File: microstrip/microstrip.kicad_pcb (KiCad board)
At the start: 2 copper layers, 50 x 50 mm, 2 parts

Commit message: Adding some changes to the design, modeling and simulation config files.
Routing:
- removed copper zone on F.Cu, net GND
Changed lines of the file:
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@@
 		(pad "" smd rect
 			(at 0 0)
-			(size 1.5 1.5)
+			(size 2.85 2.85)
 			(layers "F.Cu" "F.Mask")
 			(net 2 "50R")
@@
 		(pad "" smd rect
 			(at 0 0)
-			(size 1.5 1.5)
+			(size 2.85 2.85)
 			(layers "F.Cu" "F.Mask")
 			(net 2 "50R")
@@
 		(end 89.445 75)
 		(stroke
-			(width 1.275)
+			(width 2.85)
 			(type solid)
 		)
@@
 		(layer "Dwgs.User")
 		(pts
-			(xy 83.78 75.64) (xy 83.78 75.89)
-		)
-		(height 19.63)
-		(orientation 1)
-		(format
-			(prefix "")
-			(suffix "mm")
-			(units 3)
-			(units_format 0)
-			(precision 4)
-			(suppress_zeroes yes)
-		)
-		(style
-			(thickness 0.2)
-			(arrow_length 1.27)
-			(text_position_mode 2)
-			(arrow_direction outward)
-			(extension_height 0.58642)
-			(extension_offset 0.5)
-			(keep_text_aligned yes)
-		)
-		(gr_text "0.25mm"
-			(at 105.46 75.74 90)
-			(layer "Dwgs.User")
-			(effects
-				(font
-					(size 1.5 1.5)
-					(thickness 0.3)
-				)
-			)
-		)
-	)
-	(dimension
-		(type orthogonal)
-		(layer "Dwgs.User")
-		(pts
-			(xy 62.54 74.36) (xy 62.54 75.64)
+			(xy 58.430002 73.574998) (xy 58.429968 76.425074)
 		)
 		(height -17.54)
@@
 			(units 3)
 			(units_format 0)
-			(precision 5)
-			(override_value "1.275")
+			(precision 2)
+			(suppress_zeroes yes)
 		)
 		(style
@@
 			(keep_text_aligned yes)
 		)
-		(gr_text "1.275mm"
-			(at 43.2 75 90)
+		(gr_text "2.85mm"
+			(at 39.090002 75.000036 90)
 			(layer "Dwgs.User")
 			(effects
@@
 		(net_name "GND")
 		(locked yes)
-		(layers "F.Cu" "B.Cu")
+		(layer "B.Cu")
 		(name "gnd_plane")
 		(hatch edge 0.5)

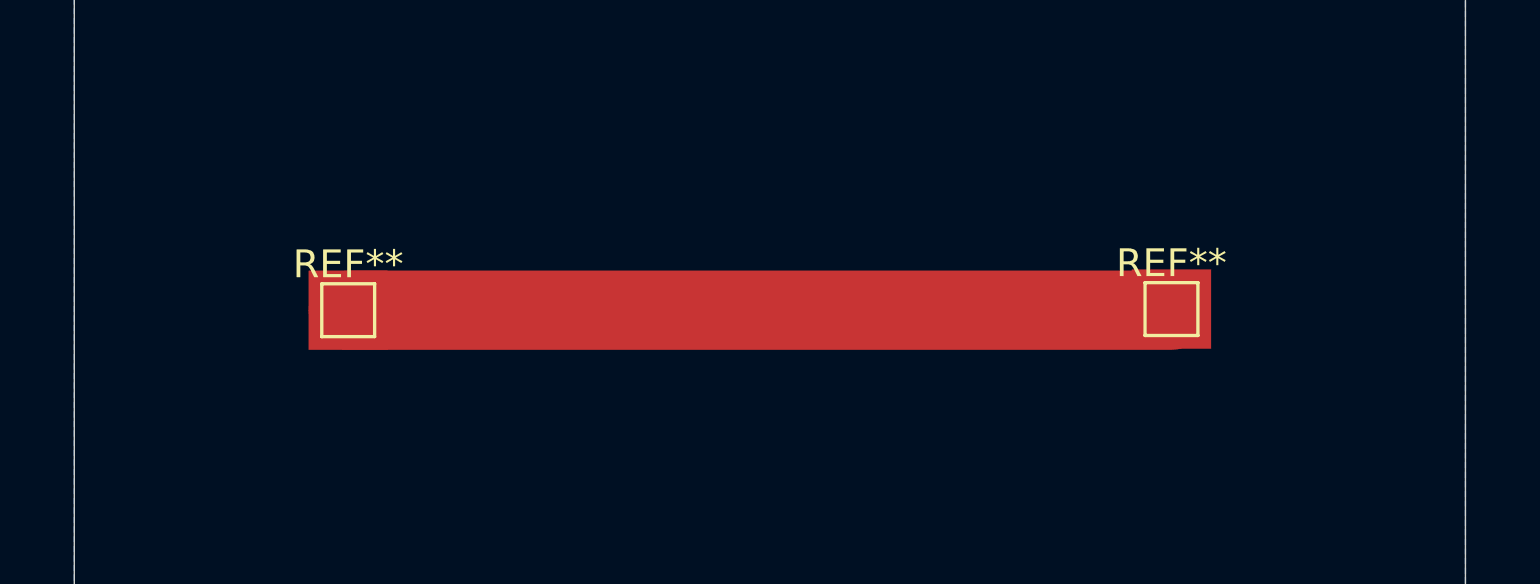
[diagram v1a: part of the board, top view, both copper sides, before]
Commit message: Creating the Emerge simulation model.
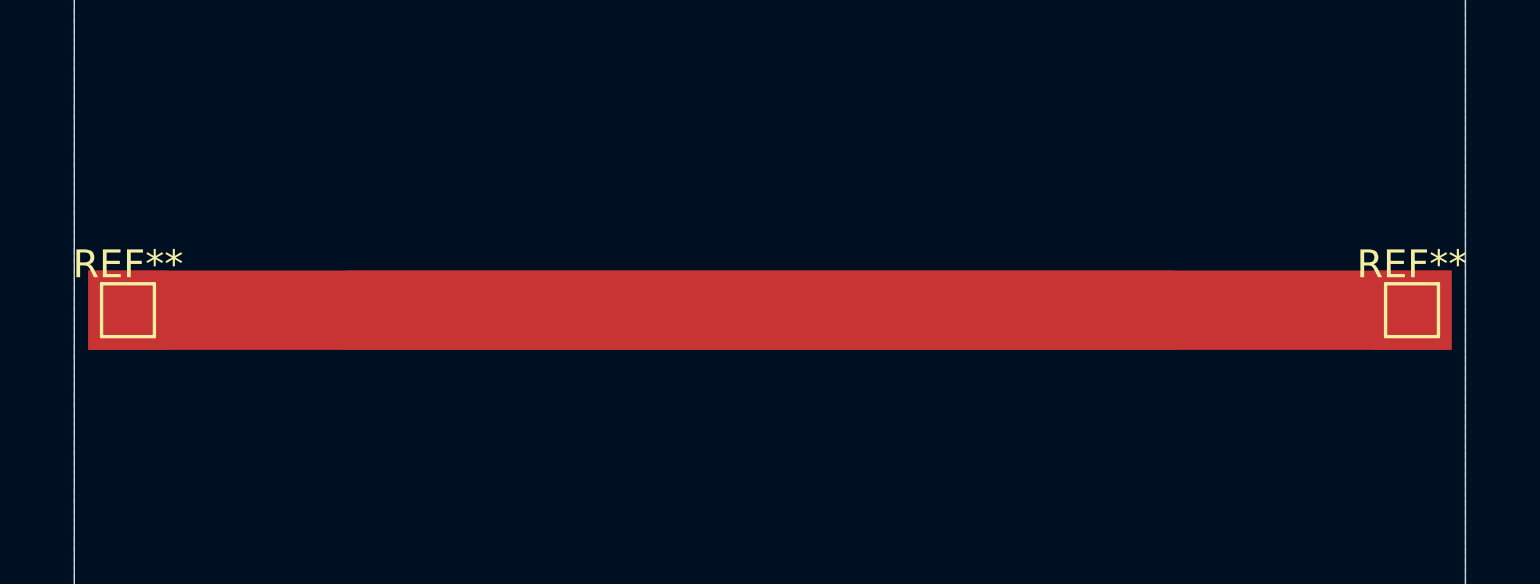
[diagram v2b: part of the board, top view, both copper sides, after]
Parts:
- moved REF** 8.65 mm to (98.1, 75.0)
- moved REF** 7.91 mm to (51.9, 75.0)
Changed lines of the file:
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@@
 	(footprint "TestPoint:TestPoint_Pad_1.5x1.5mm"
 		(layer "F.Cu")
-		(at 89.445 74.96)
+		(at 98.09 75)
 		(descr "SMD rectangular pad as test Point, square 1.5mm side length")
 		(tags "test point SMD pad rectangle square")
@@
 			(at 0 0)
 			(size 2.85 2.85)
-			(layers "F.Cu" "F.Mask")
+			(layers "F.Cu")
 			(net 2 "50R")
 		)
@@
 	(footprint "TestPoint:TestPoint_Pad_1.5x1.5mm"
 		(layer "F.Cu")
-		(at 59.855 75)
+		(at 51.94 75)
 		(descr "SMD rectangular pad as test Point, square 1.5mm side length")
 		(tags "test point SMD pad rectangle square")
@@
 			(at 0 0)
 			(size 2.85 2.85)
-			(layers "F.Cu" "F.Mask")
+			(layers "F.Cu")
 			(net 2 "50R")
 		)
@@
 			(type solid)
 		)
+		(layer "F.Cu")
+		(net 2)
+	)
+	(gr_rect
+		(start 50.51 73.575)
+		(end 99.51 76.425)
+		(stroke
+			(width 0)
+			(type default)
+		)
+		(fill yes)
 		(layer "F.Cu")
 		(net 2)
@@
 		(layer "Dwgs.User")
 		(pts
-			(xy 58.430002 73.574998) (xy 58.429968 76.425074)
+			(xy 50.51 76.425074) (xy 50.51 73.575)
 		)
 		(height -17.54)
@@
 		)
 		(gr_text "2.85mm"
-			(at 39.090002 75.000036 90)
+			(at 31.17 75.000037 90)
 			(layer "Dwgs.User")
 			(effects
